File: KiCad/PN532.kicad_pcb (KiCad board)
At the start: 2 copper layers, 42 x 42 mm, 55 parts, among them J1 Bell, J2 Header, J3 SPOX, SW1 TAMPER, U1 PN532, U2 QR, Y1 27.12MHz

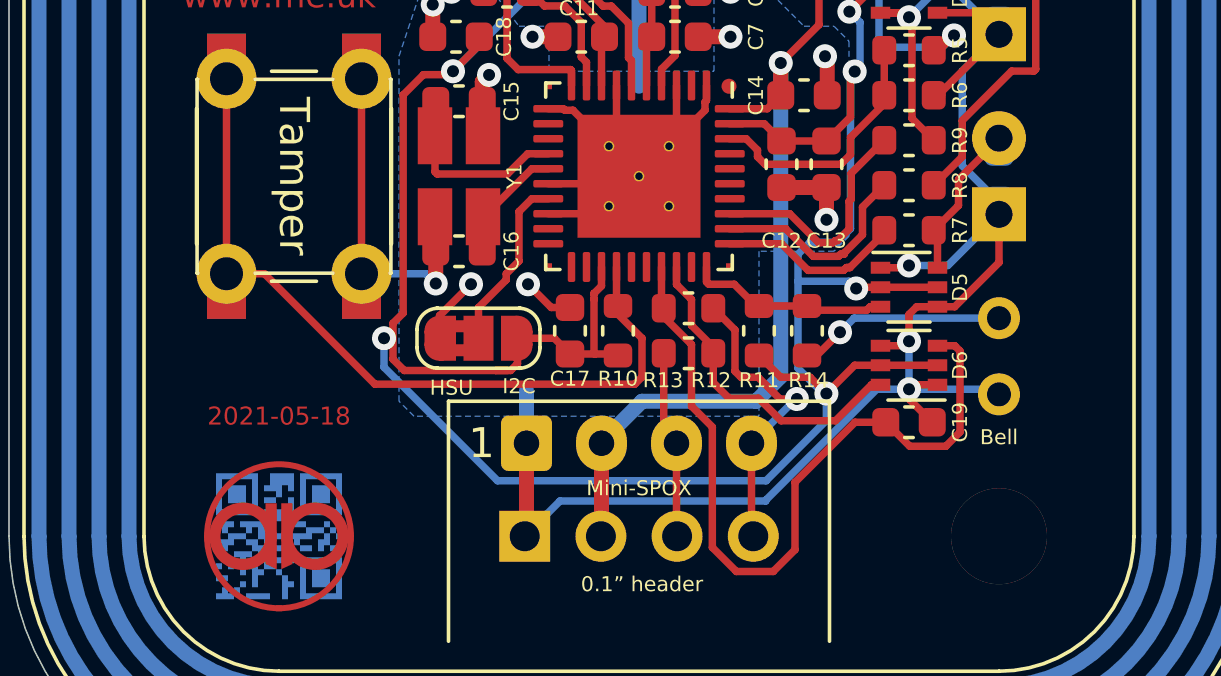
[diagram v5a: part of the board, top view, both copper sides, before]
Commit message: Holes for bell pins fixed
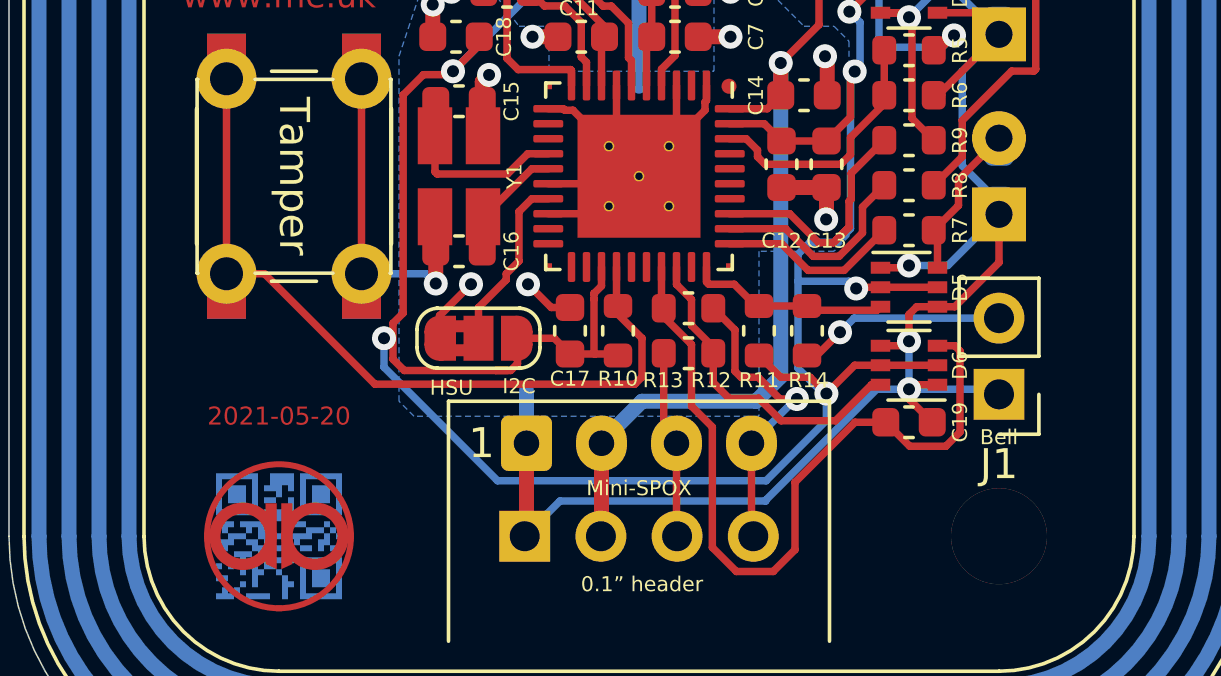
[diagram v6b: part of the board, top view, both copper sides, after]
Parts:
- J1: footprint TestPoint:TestPoint_2Pads_Pitch2.54mm_Drill0.8mm -> Connector_PinHeader_2.54mm:PinHeader_1x02_P2.54mm_Vertical; moved to F.Cu
- turned J1 to 180 degrees
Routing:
- net Net-(R9-Pad1): track 8.01 -> 8.60 mm
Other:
- board text added: "2021-05-20"
- board text removed: "2021-05-18"

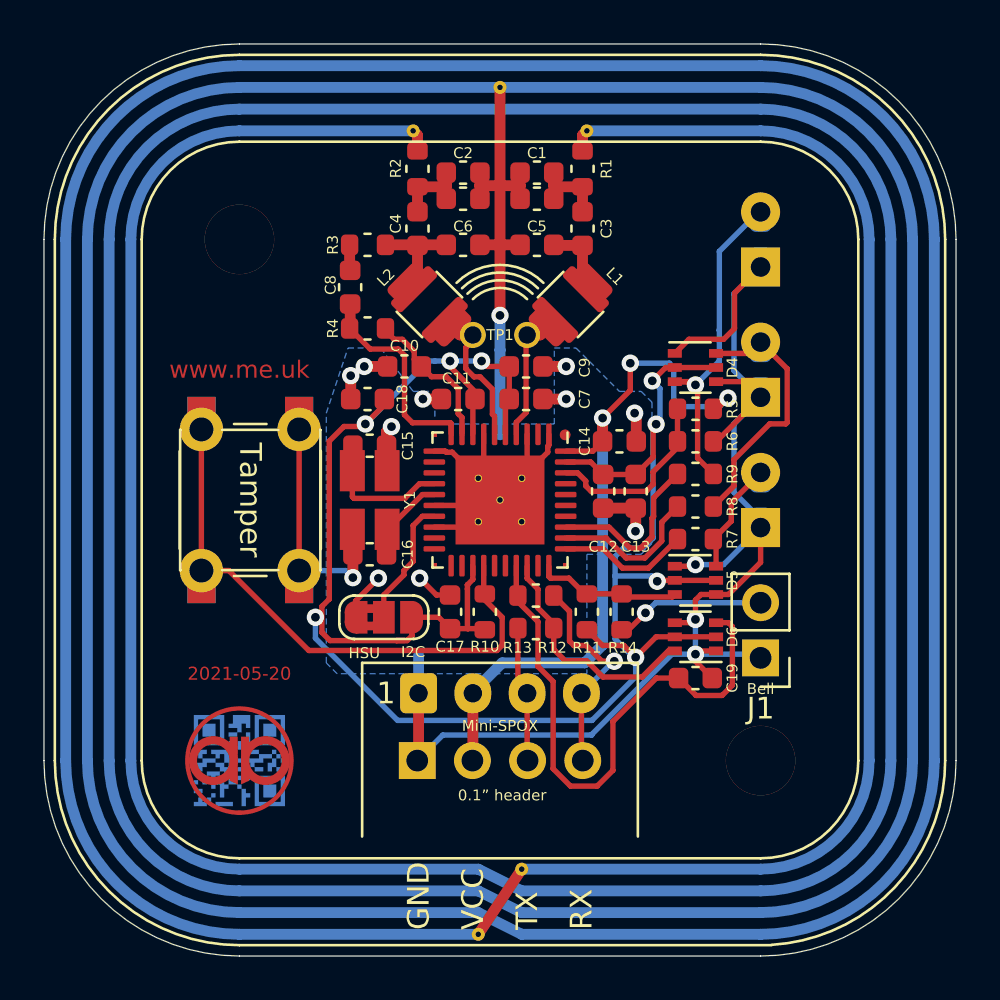
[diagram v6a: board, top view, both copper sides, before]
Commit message: Minor tweak around LEDs
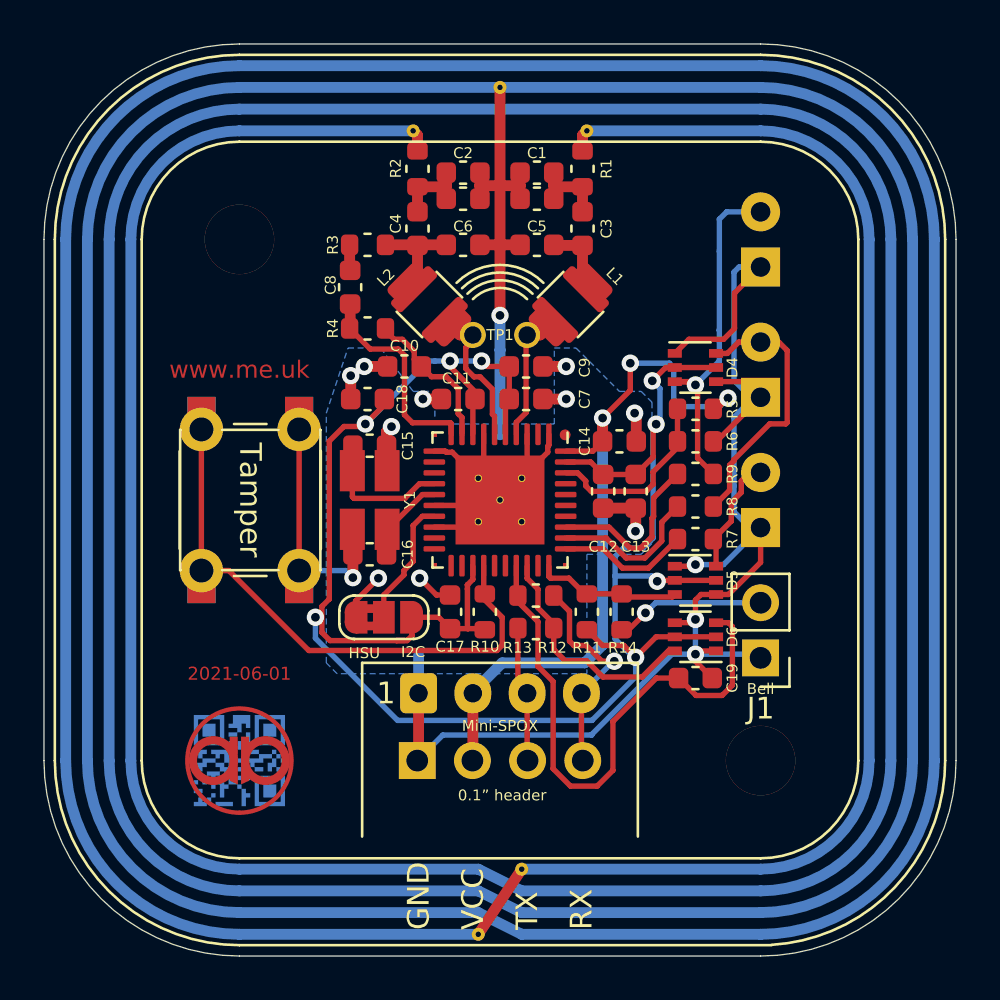
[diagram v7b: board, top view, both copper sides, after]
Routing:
- net GND: track 127.3 -> 129.0 mm
- net Net-(D3-Pad2): track 15.4 -> 16.5 mm
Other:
- board text added: "2021-06-01"
- board text removed: "2021-05-20"

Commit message: Slot for reverse LED mounting option
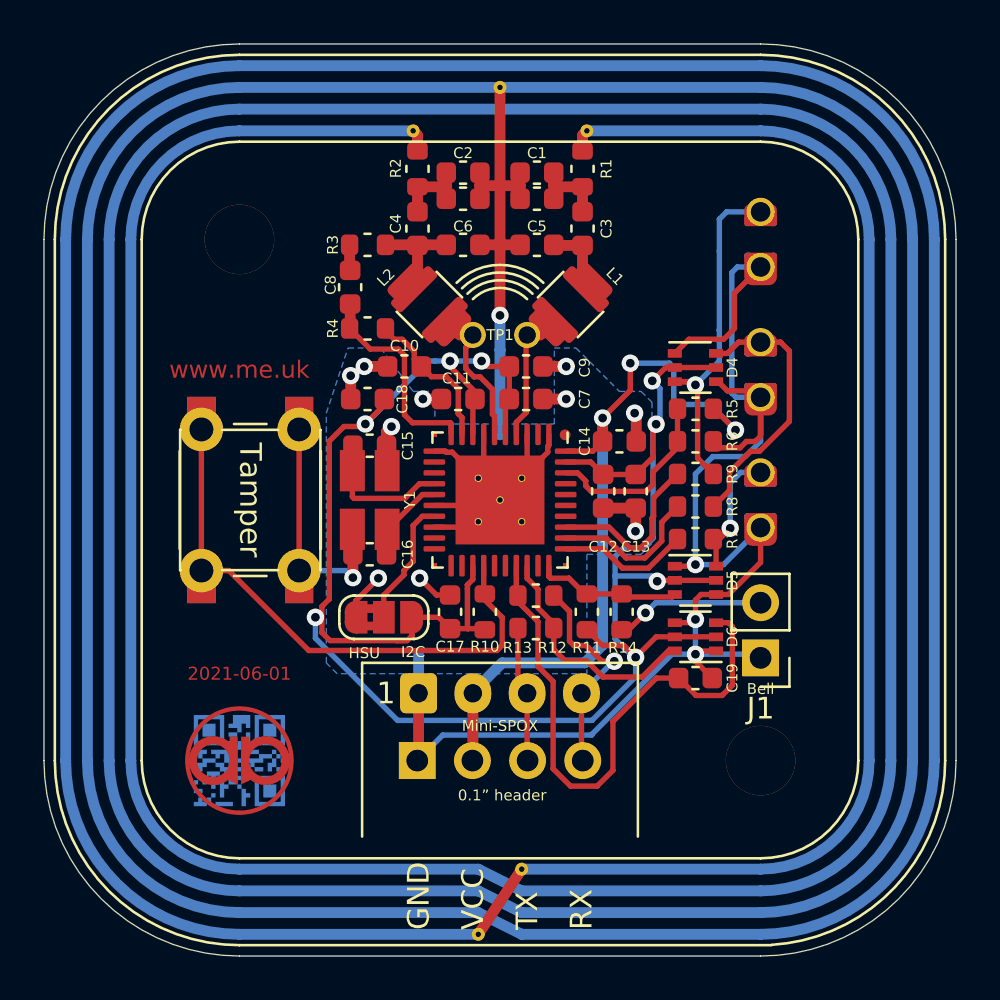
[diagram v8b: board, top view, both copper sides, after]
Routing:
- net GND: track 129.0 -> 133.3 mm
- net +5V: track 33.7 -> 34.9 mm
- net Net-(D1-Pad2): track 5.57 -> 5.97 mm, vias 0 -> 1
